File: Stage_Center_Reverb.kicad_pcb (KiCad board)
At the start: 2 copper layers, 68.6 x 46.4 mm, 31 parts, among them Q1 2N3906, U1 TL072, U2 TL072, U3 MAX1044

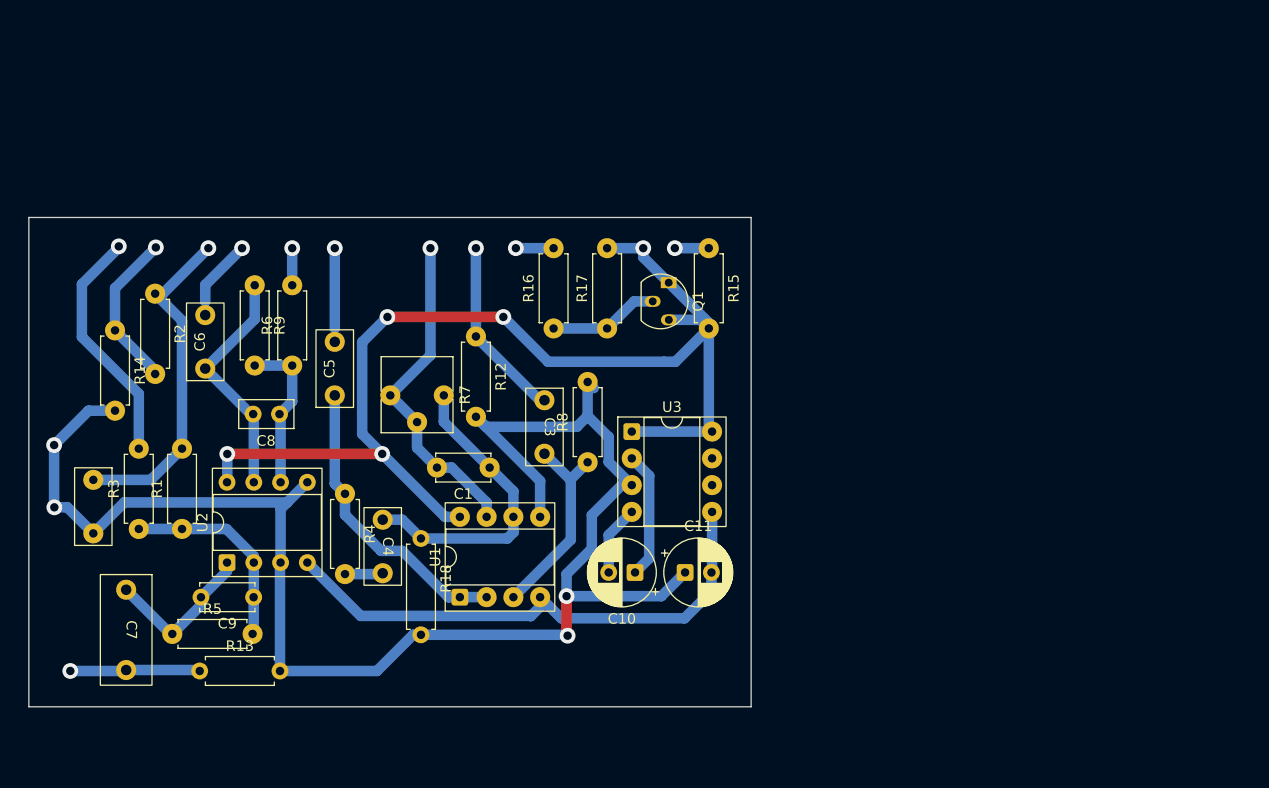
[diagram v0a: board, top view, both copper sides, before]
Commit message: フットプリント修正、LEDの抵抗を可変に変更
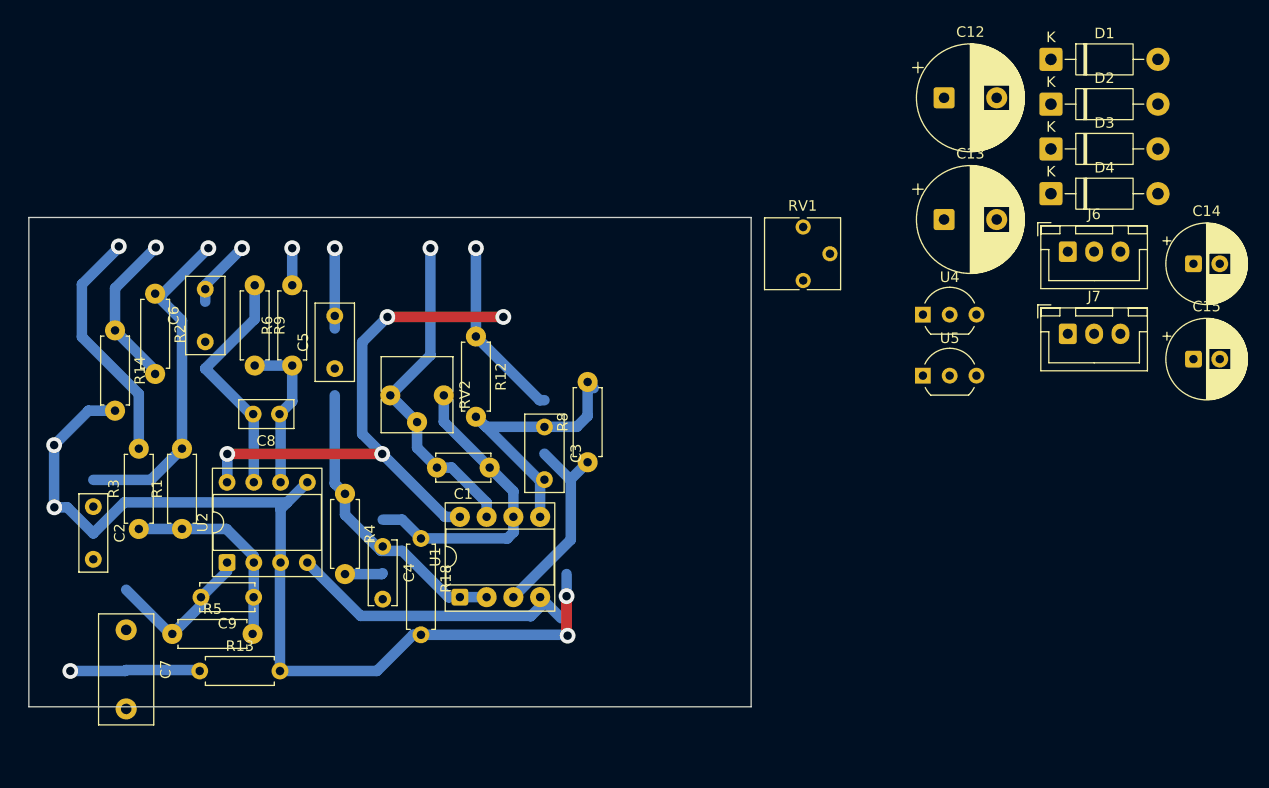
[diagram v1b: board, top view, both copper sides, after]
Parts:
- removed C10, C11: 10uF, Capacitor_THT:CP_Radial_D6.3mm_P2.50mm
- removed Q1: 2N3906, Package_TO_SOT_THT:TO-92_Inline
- removed R15, R17: 1k, Resistor_THT:R_Axial_DIN0207_L6.3mm_D2.5mm_P7.62mm_Horizontal
- removed R16: 6k8, Resistor_THT:R_Axial_DIN0207_L6.3mm_D2.5mm_P7.62mm_Horizontal
- removed U3: MAX1044, Package_DIP:DIP-8_W7.62mm_Socket
- added C12: 25V1000uF, Capacitor_THT:CP_Radial_D10.0mm_P5.00mm, F.Cu at (180.8, 63.2)
- added C13: 25V1000uF, Capacitor_THT:CP_Radial_D10.0mm_P5.00mm, F.Cu at (180.8, 74.8)
- added C14: 25V100uF, Capacitor_THT:CP_Radial_D7.5mm_P2.50mm, F.Cu at (204.5, 79.0)
- added C15: 25V100uF, Capacitor_THT:CP_Radial_D7.5mm_P2.50mm, F.Cu at (204.5, 88.0)
- added D1: 30V1A, Diode_THT:D_DO-41_SOD81_P10.16mm_Horizontal, F.Cu at (191.0, 59.5)
- added D2: 30V1A, Diode_THT:D_DO-41_SOD81_P10.16mm_Horizontal, F.Cu at (191.0, 63.8)
- added D3: 30V1A, Diode_THT:D_DO-41_SOD81_P10.16mm_Horizontal, F.Cu at (191.0, 68.0)
- added D4: 30V1A, Diode_THT:D_DO-41_SOD81_P10.16mm_Horizontal, F.Cu at (191.0, 72.3)
- added J6: Conn_01x03, Connector_JST:JST_XH_B3B-XH-A_1x03_P2.50mm_Vertical, F.Cu at (192.6, 77.8)
- added J7: Conn_01x03, Connector_JST:JST_XH_B3B-XH-A_1x03_P2.50mm_Vertical, F.Cu at (192.6, 85.6)
- added RV1: 1k, Potentiometer_THT:Potentiometer_Vishay_T73YP_Vertical, F.Cu at (167.5, 80.5)
- added U4: L78L15, Package_TO_SOT_THT:TO-92_Inline_Wide, F.Cu at (178.8, 83.8)
- added U5: L79L15, Package_TO_SOT_THT:TO-92_Inline_Wide, F.Cu at (178.8, 89.6)
- C2: footprint @MyLibrary:7.5_3.5_p5.0 -> Capacitor_THT:C_Rect_L7.2mm_W2.5mm_P5.00mm_FKS2_FKP2_MKS2_MKP2
- C3, C5, C6: footprint @MyLibrary:7.5_3.5_p5.0 -> Capacitor_THT:C_Rect_L7.2mm_W3.5mm_P5.00mm_FKS2_FKP2_MKS2_MKP2
- C4: value 1500pF -> 1000pF; footprint @MyLibrary:7.5_3.5_p5.0 -> Capacitor_THT:C_Disc_D6.0mm_W2.5mm_P5.00mm
- C7: footprint @MyLibrary:10.5_5.0_p7.5 -> Capacitor_THT:C_Rect_L10.3mm_W5.0mm_P7.50mm_MKS4
- C8: value 220pF -> 30pF
- RV2: renamed from R7; value 500k -> 1M
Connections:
- net +9V renamed +15V
- net -9V renamed -15V
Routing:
- net +15V: track 111.7 -> 53.3 mm, vias 5 -> 4
- net GNDPWR: track 151.0 -> 118.9 mm
- net -15V: track 51.2 -> 28.3 mm
- net Net-(U3-CAP+): track 12.1 -> 0.00 mm
- net Net-(Q1-B): track 10.5 -> 0.00 mm
- net Net-(U3-CAP-): track 6.66 -> 0.00 mm
- net Net-(J1-PadS): track 3.58 -> 0.00 mm, vias 1 -> 0
- net Net-(D3-A): track 3.22 -> 0.00 mm, vias 1 -> 0

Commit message: 電源をトランスから正負15Vを作るように変更 コネクタ等との接続をXHコネクタを使うよう変更
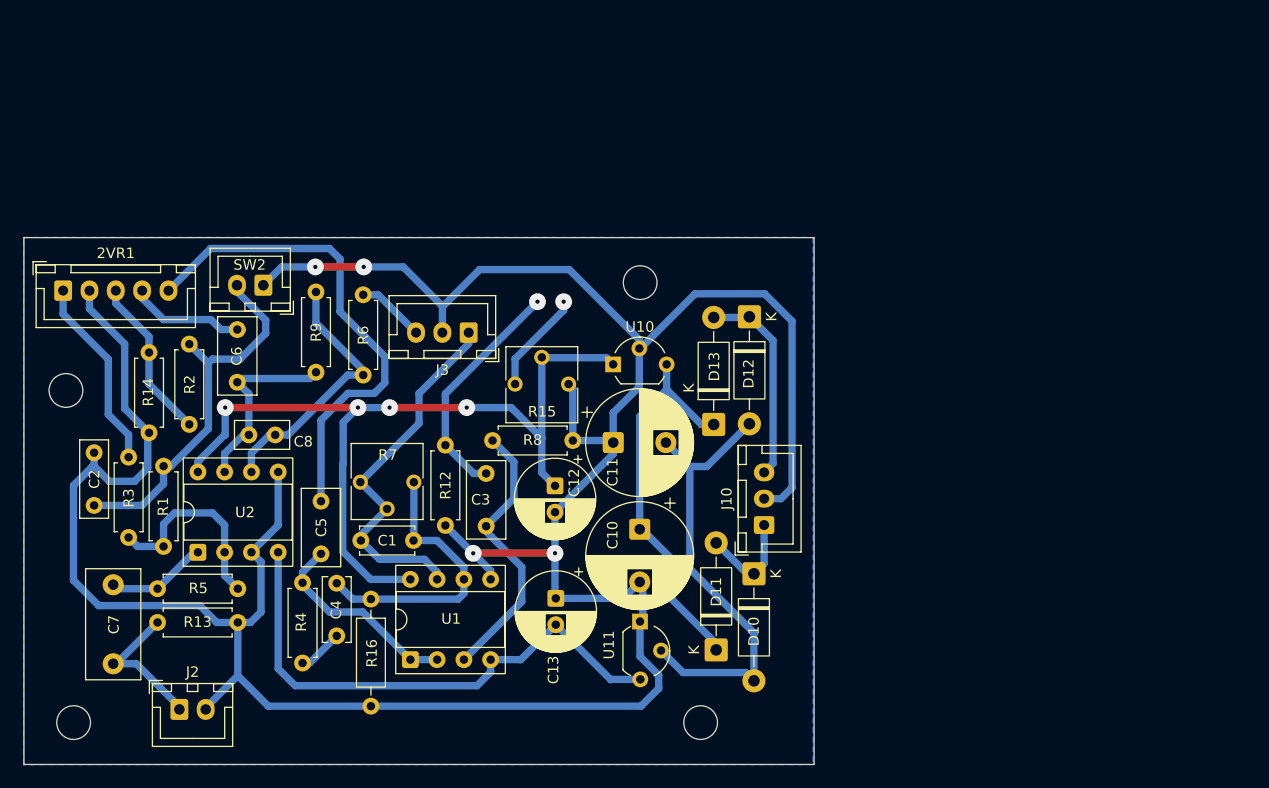
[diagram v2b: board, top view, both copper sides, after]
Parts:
- removed C14, C15: 25V100uF, Capacitor_THT:CP_Radial_D7.5mm_P2.50mm
- removed C9: 470pF, Capacitor_THT:C_Disc_D5.0mm_W2.5mm_P5.00mm
- removed D1, D2, D3, D4: 30V1A, Diode_THT:D_DO-41_SOD81_P10.16mm_Horizontal
- removed J6, J7: Conn_01x03, Connector_JST:JST_XH_B3B-XH-A_1x03_P2.50mm_Vertical
- removed R18: 330k, Resistor_THT:R_Axial_DIN0207_L6.3mm_D2.5mm_P7.62mm_Horizontal
- removed RV1: 1k, Potentiometer_THT:Potentiometer_Vishay_T73YP_Vertical
- removed RV2: 1M, Potentiometer_THT:Potentiometer_Vishay_T73YP_Vertical
- removed U4: L78L15, Package_TO_SOT_THT:TO-92_Inline_Wide
- removed U5: L79L15, Package_TO_SOT_THT:TO-92_Inline_Wide
- added 2VR1: A50k, Connector_JST:JST_XH_B5B-XH-A_1x05_P2.50mm_Vertical, F.Cu at (97.2, 81.5)
- added C10: 25V1000uF, Capacitor_THT:CP_Radial_D10.0mm_P5.00mm, F.Cu at (151.9, 104.2)
- added C11: 25V1000uF, Capacitor_THT:CP_Radial_D10.0mm_P5.00mm, F.Cu at (149.4, 95.9)
- added D10: 30V1A, Diode_THT:D_DO-41_SOD81_P10.16mm_Horizontal, F.Cu at (162.8, 108.4)
- added D11: 30V1A, Diode_THT:D_DO-41_SOD81_P10.16mm_Horizontal, F.Cu at (159.2, 115.6)
- added D12: 30V1A, Diode_THT:D_DO-41_SOD81_P10.16mm_Horizontal, F.Cu at (162.4, 84.0)
- added D13: 30V1A, Diode_THT:D_DO-41_SOD81_P10.16mm_Horizontal, F.Cu at (159.0, 94.2)
- added H1: MountingHole, MountingHole:MountingHole_3.2mm_M3, F.Cu at (97.5, 91.0)
- added H2: MountingHole, MountingHole:MountingHole_3.2mm_M3, F.Cu at (152.0, 80.7)
- added H3: MountingHole, MountingHole:MountingHole_3.2mm_M3, F.Cu at (98.2, 122.5)
- added H4: MountingHole, MountingHole:MountingHole_3.2mm_M3, F.Cu at (157.7, 122.5)
- added J10: Power, Connector_JST:JST_XH_B3B-XH-A_1x03_P2.50mm_Vertical, F.Cu at (163.8, 103.8)
- added J2: Output, Connector_JST:JST_XH_B2B-XH-A_1x02_P2.50mm_Vertical, F.Cu at (108.2, 121.2)
- added J3: Tank, Connector_JST:JST_XH_B3B-XH-A_1x03_P2.50mm_Vertical, F.Cu at (135.7, 85.5)
- added R15: 1k, Potentiometer_THT:Potentiometer_Vishay_T73YP_Vertical, F.Cu at (145.2, 90.4)
- added R16: 330k, Resistor_THT:R_Axial_DIN0207_L6.3mm_D2.5mm_P10.16mm_Horizontal, F.Cu at (126.4, 110.8)
- added R7: 1M, Potentiometer_THT:Potentiometer_Vishay_T73YP_Vertical, F.Cu at (125.4, 99.7)
- added SW2: kill, Connector_JST:JST_XH_B2B-XH-A_1x02_P2.50mm_Vertical, F.Cu at (116.2, 81.0)
- added U10: L78L15, Package_TO_SOT_THT:TO-92_Inline_Wide, F.Cu at (149.4, 88.5)
- added U11: L79L15, Package_TO_SOT_THT:TO-92_Inline_Wide, F.Cu at (152.2, 113.2)
- C12, C13: value 25V1000uF -> 25V100uF; footprint Capacitor_THT:CP_Radial_D10.0mm_P5.00mm -> Capacitor_THT:CP_Radial_D7.5mm_P2.50mm
- C6: value 1500pF -> 0.47uF
- moved C12 52.2 mm to (143.9, 100.0), turned to -90 degrees
- moved C13 51.5 mm to (144.0, 110.7), turned to -90 degrees
- moved C5 17.6 mm to (121.7, 106.5)
- moved R12 10.7 mm to (133.5, 96.2)
- moved R9 10.1 mm to (121.2, 89.2), turned to 90 degrees
- moved C1 10.0 mm to (130.5, 105.2)
- moved R4 9.35 mm to (119.9, 109.2)
- moved R8 9.26 mm to (138.0, 95.7), turned to 0 degrees
- moved U1 7.57 mm to (130.2, 116.5)
- moved C3 7.08 mm to (137.4, 98.9)
- moved R6 6.80 mm to (125.7, 89.5)
- moved R13 6.10 mm to (106.2, 113.0)
- moved R2 5.78 mm to (109.2, 86.6)
- moved C4 5.59 mm to (123.2, 109.3)
- moved C6 4.89 mm to (113.7, 90.2)
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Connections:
- C12 pad 1: Net-(D2-K) -> +15V
- C13 pad 2: Net-(D1-A) -> -15V
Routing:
- net GNDPWR: track 118.9 -> 278.1 mm
- net Net-(D10-A): track 0.00 -> 43.6 mm
- net Net-(2VR1-Pad1): track 7.62 -> 47.1 mm, vias 1 -> 0
- net Net-(D11-K): track 0.00 -> 37.3 mm
- net +15V: track 53.3 -> 79.7 mm
- net -15V: track 28.3 -> 51.3 mm
- net Net-(D12-K): track 0.00 -> 19.9 mm
- net Net-(D10-K): track 0.00 -> 10.8 mm
- net Net-(D1-A): track 0.00 -> 9.80 mm, vias 0 -> 1
- net Net-(U2B--): track 15.3 -> 24.9 mm
- net Net-(U1A--): track 28.2 -> 19.4 mm
- net Net-(U1A-+): track 19.3 -> 25.7 mm
- net Net-(C7-Pad1): track 15.0 -> 9.63 mm
- net Net-(C6-Pad1): track 22.7 -> 17.7 mm
- net Net-(2VR1-Pad4): track 6.53 -> 11.5 mm, vias 1 -> 0
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- added copper zone on B.Cu, net GNDPWR
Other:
- board size 68.6 x 46.4 mm -> 75 x 50 mm

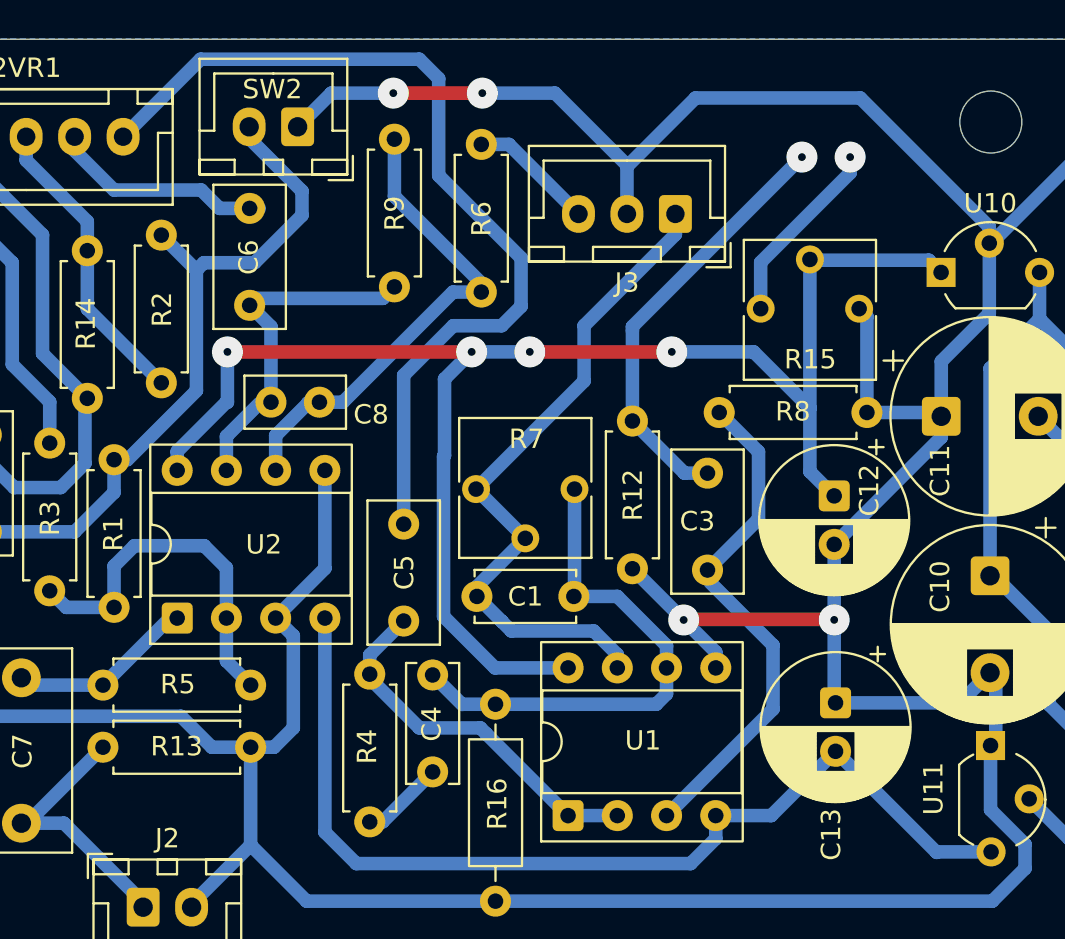
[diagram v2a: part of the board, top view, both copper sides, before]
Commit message: エッチングのため配線が狭いところを修正
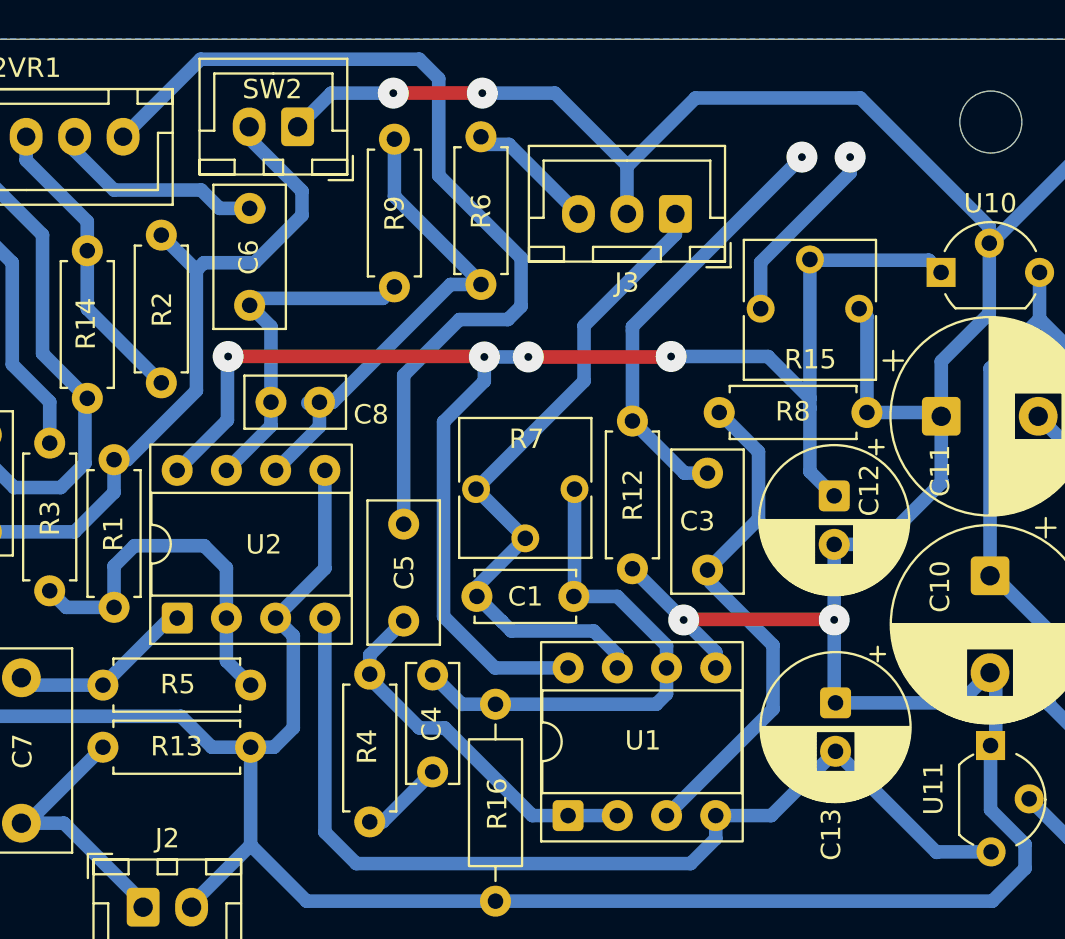
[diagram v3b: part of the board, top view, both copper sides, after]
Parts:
- moved R6 0.39 mm to (125.7, 89.1)
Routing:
- net GNDPWR: track 278.1 -> 279.5 mm

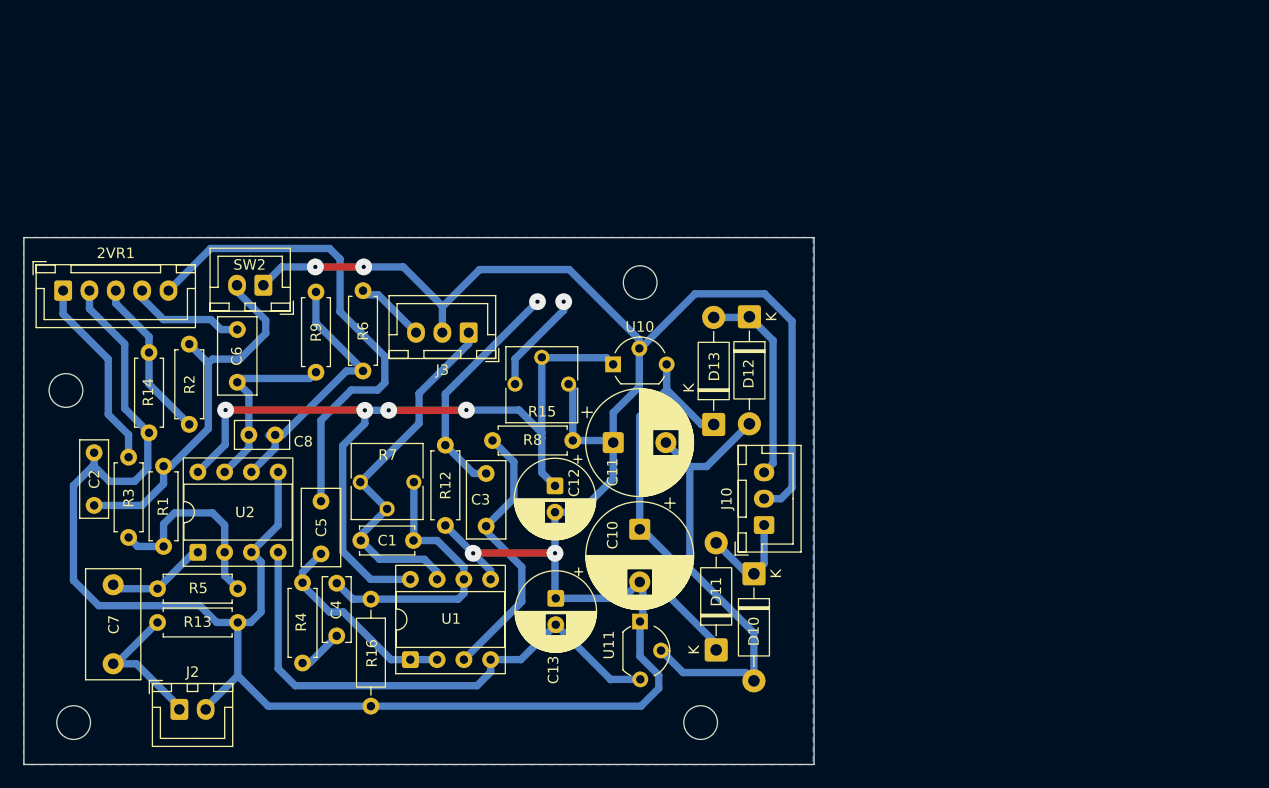
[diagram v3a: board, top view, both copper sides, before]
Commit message: 電元部分の電解コンデンサを35Vに変更 ICを抜きやすいよう配置を修正
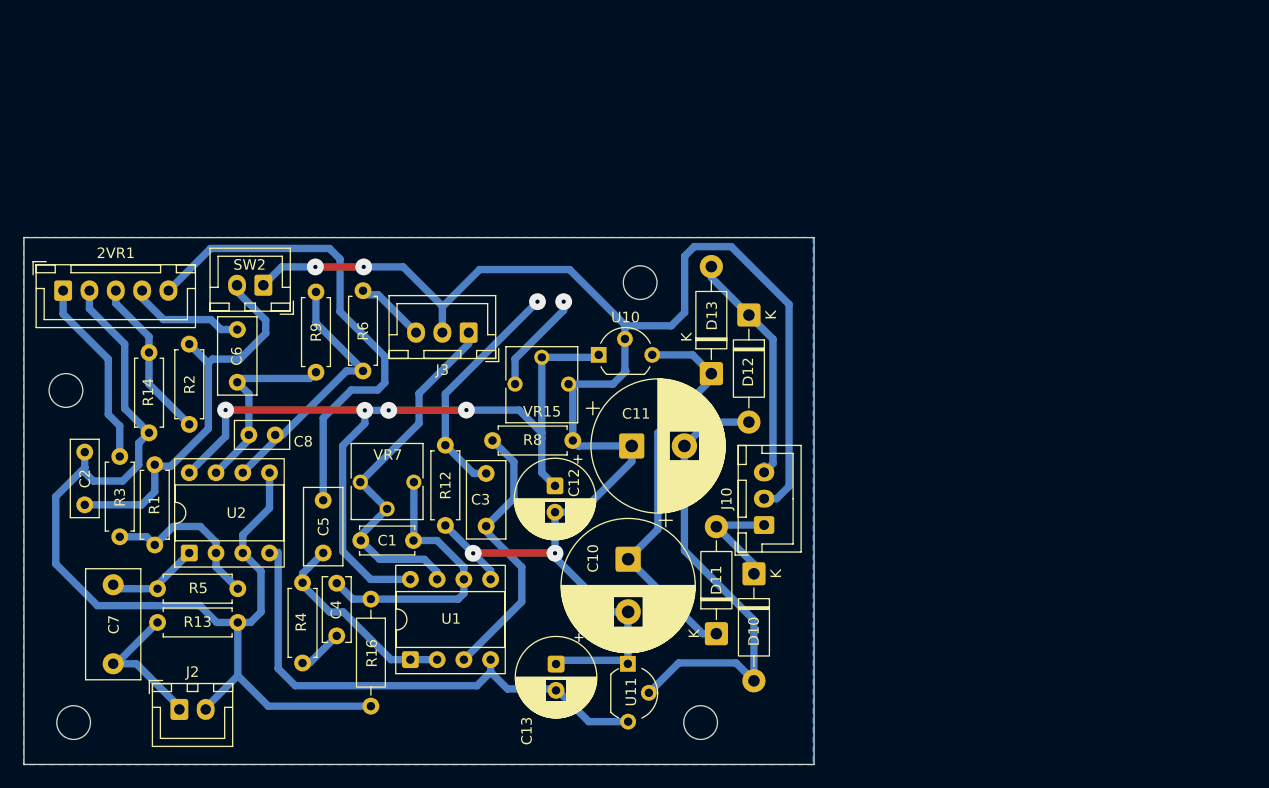
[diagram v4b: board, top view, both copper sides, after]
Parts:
- C10, C11: value 25V1000uF -> 35V1000uF; footprint Capacitor_THT:CP_Radial_D10.0mm_P5.00mm -> Capacitor_THT:CP_Radial_D12.5mm_P5.00mm
- moved C13 6.24 mm to (144.0, 116.9)
- moved D13 4.83 mm to (158.7, 89.4)
- moved U11 4.18 mm to (151.0, 117.2)
- moved C10 3.05 mm to (150.8, 107.0)
- moved C11 1.78 mm to (151.2, 96.2)
- moved U10 1.64 mm to (148.1, 87.6)
- moved D11 1.54 mm to (159.2, 114.1)
- moved C2 0.89 mm to (99.3, 101.8)
- moved R1 0.85 mm to (105.9, 105.6)
- moved R3 0.84 mm to (102.6, 104.9)
- moved U2 0.82 mm to (109.2, 106.4)
- moved C5 0.23 mm to (121.9, 106.4)
- moved D12 0.17 mm to (162.3, 83.8)
- renumbered R15 to VR15, R7 to VR7
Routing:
- net GNDPWR: track 279.5 -> 259.6 mm
- net Net-(D12-K): track 19.9 -> 23.4 mm
- net Net-(U2A--): track 19.1 -> 16.1 mm
- net -15V: track 51.3 -> 48.6 mm
- net Net-(D10-K): track 10.8 -> 12.2 mm
- net Net-(D11-K): track 37.3 -> 38.5 mm
- net +15V: track 79.4 -> 78.4 mm
- net Net-(C7-Pad1): track 9.63 -> 9.00 mm
- net Net-(SW2-B): track 36.2 -> 36.8 mm
- net Net-(2VR1-Pad2): track 18.5 -> 18.0 mm
